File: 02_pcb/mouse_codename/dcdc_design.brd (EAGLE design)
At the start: 45 x 50 mm, 6 parts, among them IC1 STM32F405RGT6, IC2 MPU-6050, IC3 DRV88361

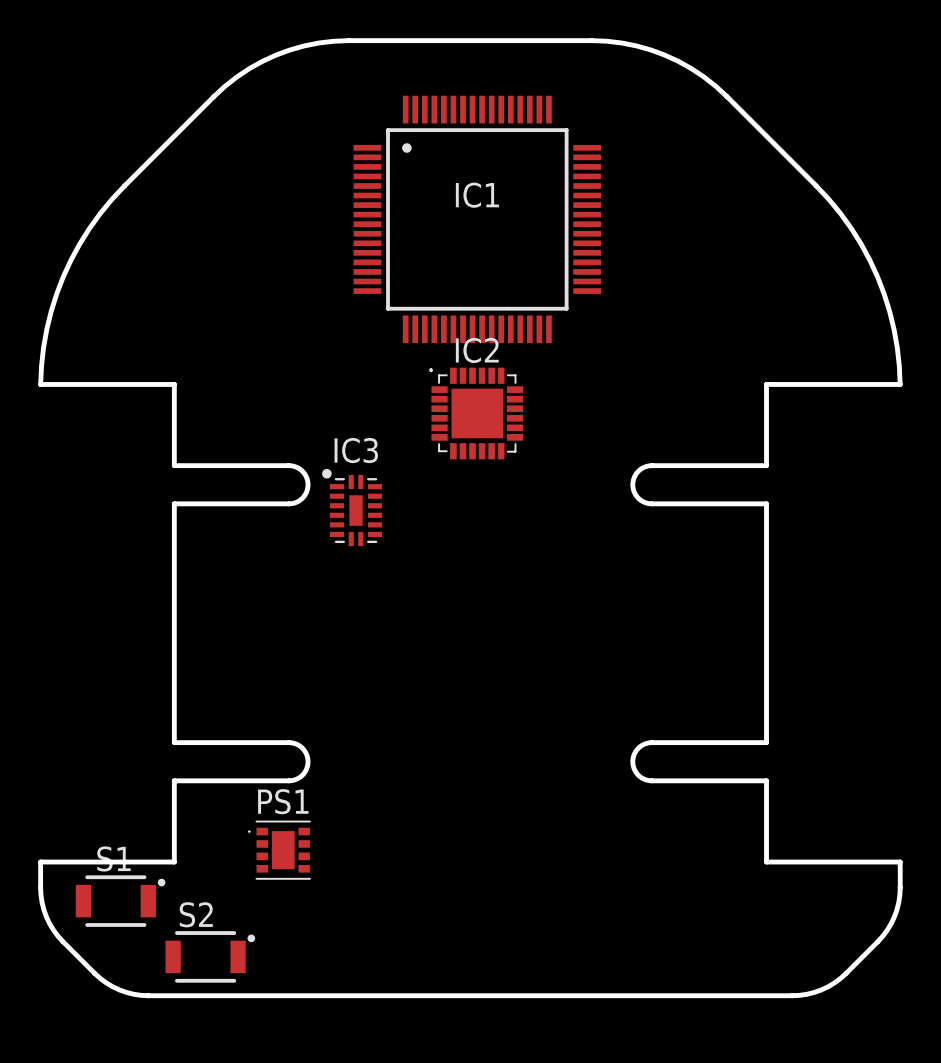
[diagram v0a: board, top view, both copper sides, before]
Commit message: eagle libraries updated, internal OC set with PLL
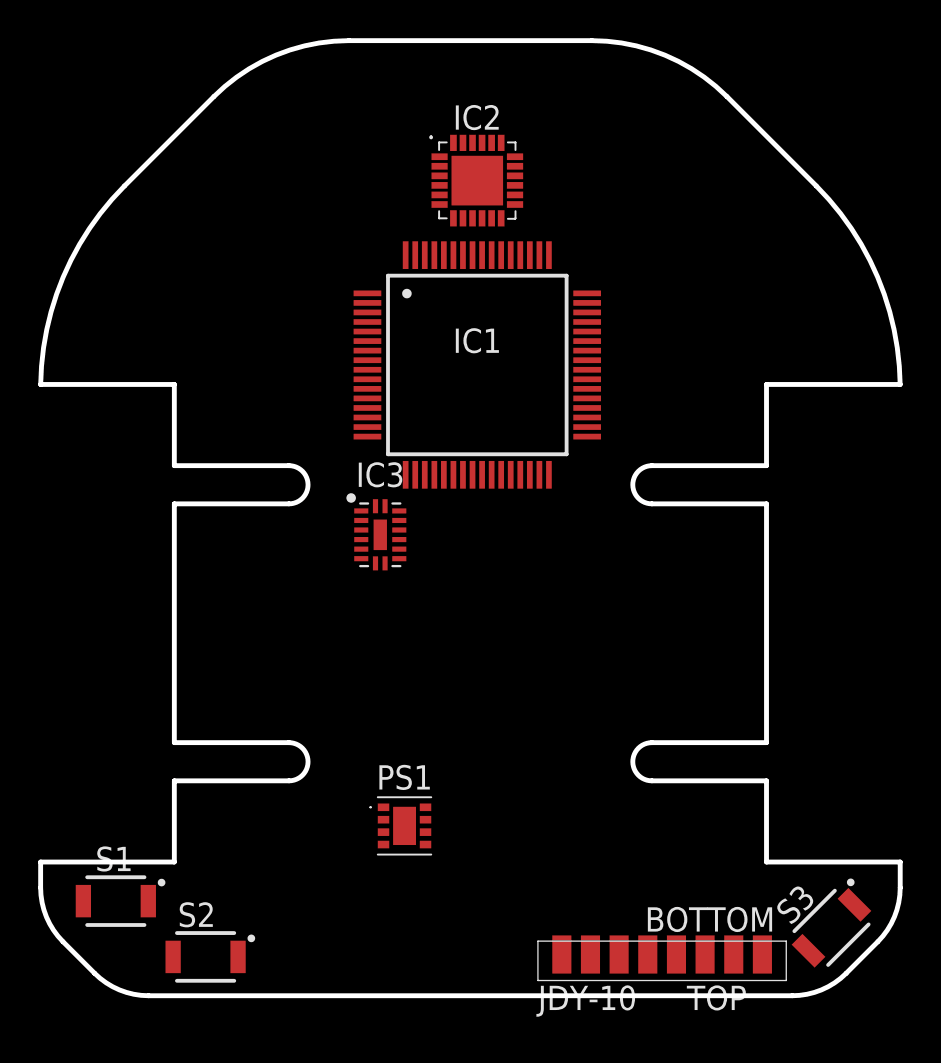
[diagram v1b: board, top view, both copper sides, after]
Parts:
- added S3: B3U-3000PB3U-3000P, parts:B3U-3000P
- added U$1: JDY-10_STANDING, parts:JDY-10_STANDING
- moved IC2 12.2 mm to (22.9, 42.7)
- moved IC1 7.62 mm to (22.9, 33.0)
- moved PS1 6.48 mm to (19.1, 8.89)
- moved IC3 1.80 mm to (17.8, 24.1)
